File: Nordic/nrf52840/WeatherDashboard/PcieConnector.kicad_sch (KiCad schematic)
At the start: 2 parts

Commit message: pcie connector
Add connectins to the pcie connector
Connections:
- net EPD_SCK: now reaches J4.14
- net EPD_DIN: now reaches J4.18
- net ~{EPD_CS}: now reaches J4.20
- net EPD_DC: now reaches J4.22
- net EPD_BUSY: now reaches J4.24
- net SDA: now reaches J4.25
- net ~{EPD_RST}: now reaches J4.26
- net SCL: now reaches J4.27
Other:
- moved on the sheet: R8
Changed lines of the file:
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@@
+	(wire
+		(pts
+			(xy 152.4 88.9) (xy 144.78 88.9)
+		)
+		(stroke
+			(width 0)
+			(type default)
+		)
+	)
 	(wire
 		(pts
@@
 	(wire
 		(pts
+			(xy 152.4 78.74) (xy 144.78 78.74)
+		)
+		(stroke
+			(width 0)
+			(type default)
+		)
+	)
+	(wire
+		(pts
+			(xy 152.4 86.36) (xy 144.78 86.36)
+		)
+		(stroke
+			(width 0)
+			(type default)
+		)
+	)
+	(wire
+		(pts
 			(xy 144.78 121.92) (xy 152.4 121.92)
 		)
@@
 	(wire
 		(pts
+			(xy 152.4 93.98) (xy 144.78 93.98)
+		)
+		(stroke
+			(width 0)
+			(type default)
+		)
+	)
+	(wire
+		(pts
+			(xy 128.27 93.98) (xy 134.62 93.98)
+		)
+		(stroke
+			(width 0)
+			(type default)
+		)
+	)
+	(wire
+		(pts
 			(xy 144.78 63.5) (xy 144.78 66.04)
 		)
@@
 	(wire
 		(pts
+			(xy 128.27 96.52) (xy 134.62 96.52)
+		)
+		(stroke
+			(width 0)
+			(type default)
+		)
+	)
+	(wire
+		(pts
 			(xy 144.78 116.84) (xy 144.78 119.38)
 		)
@@
 	(wire
 		(pts
-			(xy 162.56 73.66) (xy 162.56 72.39)
+			(xy 170.18 73.66) (xy 170.18 72.39)
 		)
 		(stroke
@@
 	(wire
 		(pts
-			(xy 144.78 81.28) (xy 162.56 81.28)
+			(xy 144.78 81.28) (xy 170.18 81.28)
 		)
 		(stroke
@@
 	(wire
 		(pts
+			(xy 152.4 83.82) (xy 144.78 83.82)
+		)
+		(stroke
+			(width 0)
+			(type default)
+		)
+	)
+	(wire
+		(pts
+			(xy 144.78 91.44) (xy 152.4 91.44)
+		)
+		(stroke
+			(width 0)
+			(type default)
+		)
+	)
+	(wire
+		(pts
 			(xy 144.78 124.46) (xy 144.78 127)
 		)
@@
 	(wire
 		(pts
-			(xy 162.56 72.39) (xy 166.37 72.39)
+			(xy 170.18 72.39) (xy 166.37 72.39)
 		)
 		(stroke
@@
 		)
 	)
+	(hierarchical_label "~{EPD_CS}"
+		(shape input)
+		(at 152.4 86.36 0)
+		(effects
+			(font
+				(size 1.27 1.27)
+			)
+			(justify left)
+		)
+	)
+	(hierarchical_label "EPD_DC"
+		(shape input)
+		(at 152.4 88.9 0)
+		(effects
+			(font
+				(size 1.27 1.27)
+			)
+			(justify left)
+		)
+	)
 	(hierarchical_label "GND"
 		(shape input)
 		(at 153.67 63.5 0)
+		(effects
+			(font
+				(size 1.27 1.27)
+			)
+			(justify left)
+		)
+	)
+	(hierarchical_label "SDA"
+		(shape input)
+		(at 128.27 93.98 180)
+		(effects
+			(font
+				(size 1.27 1.27)
+			)
+			(justify right)
+		)
+	)
+	(hierarchical_label "EPD_BUSY"
+		(shape input)
+		(at 152.4 91.44 0)
+		(effects
+			(font
+				(size 1.27 1.27)
+			)
+			(justify left)
+		)
+	)
+	(hierarchical_label "EPD_SCK"
+		(shape input)
+		(at 152.4 78.74 0)
+		(effects
+			(font
+				(size 1.27 1.27)
+			)
+			(justify left)
+		)
+	)
+	(hierarchical_label "SCL"
+		(shape input)
+		(at 128.27 96.52 180)
+		(effects
+			(font
+				(size 1.27 1.27)
+			)
+			(justify right)
+		)
+	)
+	(hierarchical_label "EPD_DIN"
+		(shape input)
+		(at 152.4 83.82 0)
+		(effects
+			(font
+				(size 1.27 1.27)
+			)
+			(justify left)
+		)
+	)
+	(hierarchical_label "~{EPD_RST}"
+		(shape input)
+		(at 152.4 93.98 0)
 		(effects
 			(font
@@
 	(symbol
 		(lib_id "Device:R_US")
-		(at 162.56 77.47 0)
+		(at 170.18 77.47 0)
 		(unit 1)
 		(exclude_from_sim no)
@@
 		(fields_autoplaced yes)
 		(property "Reference" "R8"
-			(at 165.1 76.1999 0)
+			(at 172.72 76.1999 0)
 			(effects
 				(font
@@
 		)
 		(property "Value" "10K"
-			(at 165.1 78.7399 0)
+			(at 172.72 78.7399 0)
 			(effects
 				(font
@@
 		)
 		(property "Footprint" "Resistor_SMD:R_0402_1005Metric_Pad0.72x0.64mm_HandSolder"
-			(at 163.576 77.724 90)
+			(at 171.196 77.724 90)
 			(effects
 				(font
@@
 		)
 		(property "Datasheet" "~"
-			(at 162.56 77.47 0)
+			(at 170.18 77.47 0)
 			(effects
 				(font
@@
 		)
 		(property "Description" "Resistor, US symbol"
-			(at 162.56 77.47 0)
+			(at 170.18 77.47 0)
 			(effects
 				(font

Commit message: Layout
layout update
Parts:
- added C14: C, Capacitor_SMD:C_0805_2012Metric_Pad1.18x1.45mm_HandSolder, symbol Device:C
- added J5: Conn_01x03_Pin, Connector_PinSocket_2.54mm:PinSocket_1x03_P2.54mm_Vertical, symbol Connector:Conn_01x03_Pin
- added S1: 436331045822, User_Footprint:4363X10458XX, symbol _Misc_Symbols:436331045822
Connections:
- net GND: now also C14.2, J5.3 (Pin_3), S1.4
- net at J4.16, R8.2: now also C14.1, S1.3
- net at J4.5: now also J5.1 (Pin_1)
- net at J4.7: now also J5.2 (Pin_2)
- no-connect marks 0 -> 29

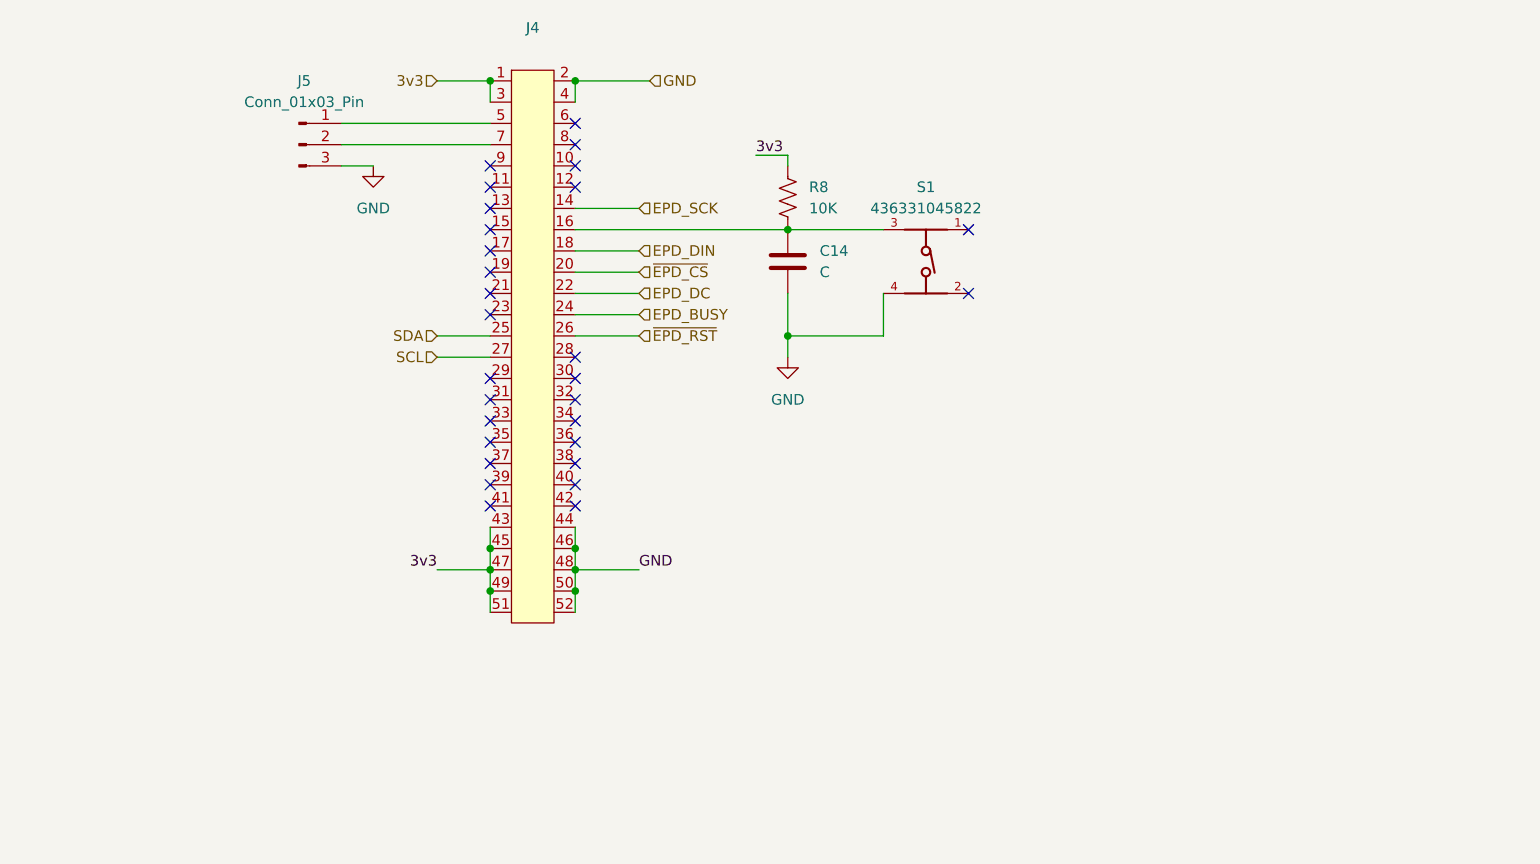
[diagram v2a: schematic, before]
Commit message: layout
Start weather station layout
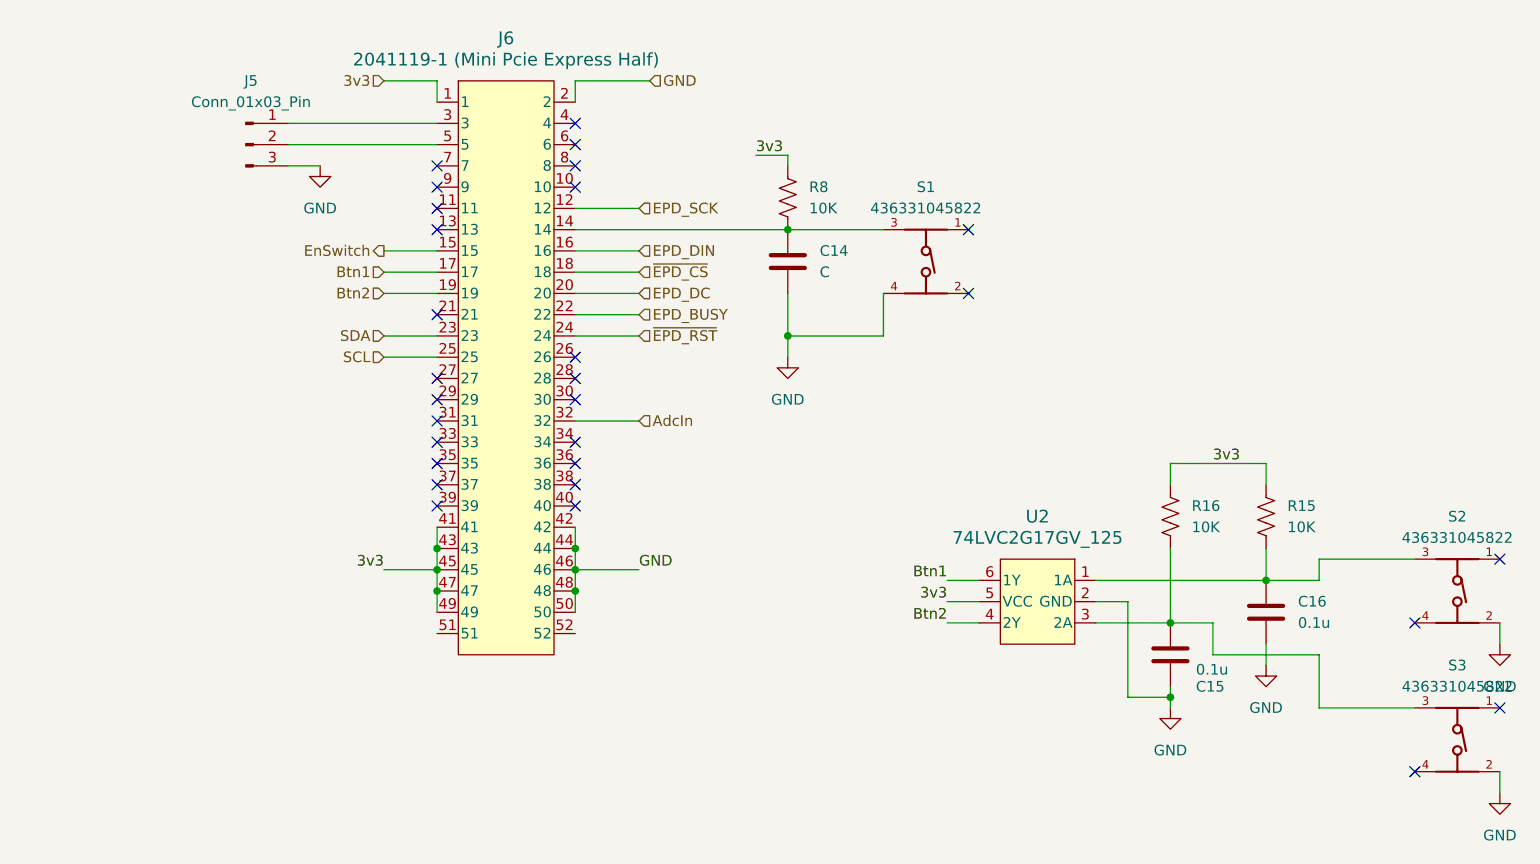
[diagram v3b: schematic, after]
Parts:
- removed J4: ~, User_Footprint:Mini PCI express Half, symbol Cards:Mini_PCIexpress_Half
- added C15, C16: 0.1u, Capacitor_SMD:C_0402_1005Metric_Pad0.74x0.62mm_HandSolder, symbol Device:C
- added J6: 2041119-1 (Mini Pcie Express Half), User_Footprint:CONN_2041119-1_TEC, symbol _Connectors:2041119-1
- added R15, R16: 10K, Resistor_SMD:R_0402_1005Metric_Pad0.72x0.64mm_HandSolder, symbol Device:R_US
- added S2, S3: 436331045822, User_Footprint:4363X10458XX, symbol _Misc_Symbols:436331045822
- added U2: 74LVC2G17GV_125, User_Footprint:SC-74_TSOP6_NEX, symbol _Misc_Symbols:74LVC2G17GV_125
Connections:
- net 3v3: now also J6.1, J6.41, J6.43, J6.45, J6.47, J6.49, R15.1, R16.1, U2.5 (VCC)
- net EPD_BUSY: now also J6.22
- net EPD_DC: now also J6.20
- net EPD_DIN: now also J6.16
- net EPD_SCK: now also J6.12
- net GND: now also C15.2, C16.2, J6.2, J6.42, J6.44, J6.46, J6.48, J6.50, S2.2, S3.2, U2.2 (GND)
- net SCL: now also J6.25
- net SDA: now also J6.23
- net ~{EPD_CS}: now also J6.18
- net ~{EPD_RST}: now also J6.24
- net at J5.1 (Pin_1): now also J6.3
- net at J5.2 (Pin_2): now also J6.5
- net at C14.1, R8.2, S1.3: now also J6.14
- new net: C16.1, R15.2, S2.3, U2.1 (1A)
- new net: C15.1, R16.2, S3.3, U2.3 (2A)
- new net AdcIn: J6.32
- new net Btn1: J6.17, U2.6 (1Y)
- new net Btn2: J6.19, U2.4 (2Y)
- new net EnSwitch: J6.15
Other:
- moved on the sheet: J5

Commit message: layout
update layout for the pcie connector
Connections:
- net EPD_BUSY: now also J6.7; no longer J6.22
- net EPD_DC: now also J6.11; no longer J6.20
- net ~{EPD_CS}: now also J6.13; no longer J6.18
- net ~{EPD_RST}: now also J6.9; no longer J6.24
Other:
- moved on the sheet: J5
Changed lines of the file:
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@@
-	)
-	(no_connect
-		(at 128.27 78.74)
 	)
 	(no_connect
@@
 	)
 	(no_connect
-		(at 128.27 73.66)
+		(at 144.78 91.44)
 	)
 	(no_connect
@@
 	)
 	(no_connect
-		(at 128.27 76.2)
+		(at 144.78 86.36)
 	)
 	(no_connect
@@
 	)
 	(no_connect
-		(at 128.27 81.28)
+		(at 144.78 88.9)
 	)
 	(no_connect
@@
 	)
 	(no_connect
+		(at 144.78 93.98)
+	)
+	(no_connect
 		(at 144.78 111.76)
 	)
@@
 	(wire
 		(pts
-			(xy 152.4 88.9) (xy 144.78 88.9)
-		)
-		(stroke
-			(width 0)
-			(type default)
-		)
-	)
-	(wire
-		(pts
 			(xy 121.92 63.5) (xy 128.27 63.5)
 		)
@@
 	(wire
 		(pts
+			(xy 121.92 78.74) (xy 128.27 78.74)
+		)
+		(stroke
+			(width 0)
+			(type default)
+		)
+	)
+	(wire
+		(pts
 			(xy 227.33 109.22) (xy 227.33 111.76)
 		)
@@
 	(wire
 		(pts
-			(xy 152.4 86.36) (xy 144.78 86.36)
-		)
-		(stroke
-			(width 0)
-			(type default)
-		)
-	)
-	(wire
-		(pts
 			(xy 144.78 121.92) (xy 152.4 121.92)
 		)
@@
 	(wire
 		(pts
-			(xy 152.4 93.98) (xy 144.78 93.98)
-		)
-		(stroke
-			(width 0)
-			(type default)
-		)
-	)
-	(wire
-		(pts
 			(xy 128.27 119.38) (xy 128.27 121.92)
 		)
@@
 	(wire
 		(pts
+			(xy 121.92 81.28) (xy 128.27 81.28)
+		)
+		(stroke
+			(width 0)
+			(type default)
+		)
+	)
+	(wire
+		(pts
 			(xy 207.01 125.73) (xy 210.82 125.73)
 		)
@@
 	(wire
 		(pts
+			(xy 121.92 76.2) (xy 128.27 76.2)
+		)
+		(stroke
+			(width 0)
+			(type default)
+		)
+	)
+	(wire
+		(pts
 			(xy 144.78 63.5) (xy 153.67 63.5)
 		)
@@
 	(wire
 		(pts
-			(xy 110.49 68.58) (xy 128.27 68.58)
+			(xy 91.44 68.58) (xy 128.27 68.58)
 		)
 		(stroke
@@
 	(wire
 		(pts
+			(xy 121.92 73.66) (xy 128.27 73.66)
+		)
+		(stroke
+			(width 0)
+			(type default)
+		)
+	)
+	(wire
+		(pts
 			(xy 215.9 111.76) (xy 215.9 109.22)
 		)
@@
 	(wire
 		(pts
-			(xy 110.49 73.66) (xy 114.3 73.66)
-		)
-		(stroke
-			(width 0)
-			(type default)
-		)
-	)
-	(wire
-		(pts
-			(xy 110.49 71.12) (xy 128.27 71.12)
+			(xy 91.44 73.66) (xy 95.25 73.66)
+		)
+		(stroke
+			(width 0)
+			(type default)
+		)
+	)
+	(wire
+		(pts
+			(xy 91.44 71.12) (xy 128.27 71.12)
 		)
 		(stroke
@@
 		(pts
 			(xy 215.9 109.22) (xy 227.33 109.22)
-		)
-		(stroke
-			(width 0)
-			(type default)
-		)
-	)
-	(wire
-		(pts
-			(xy 144.78 91.44) (xy 152.4 91.44)
 		)
 		(stroke
@@
 	(hierarchical_label "~{EPD_CS}"
 		(shape input)
-		(at 152.4 86.36 0)
+		(at 121.92 81.28 180)
+		(effects
+			(font
+				(size 1.27 1.27)
+			)
+			(justify right)
+		)
+	)
+	(hierarchical_label "EPD_DC"
+		(shape input)
+		(at 121.92 78.74 180)
+		(effects
+			(font
+				(size 1.27 1.27)
+			)
+			(justify right)
+		)
+	)
+	(hierarchical_label "Btn1"
+		(shape input)
+		(at 121.92 86.36 180)
+		(effects
+			(font
+				(size 1.27 1.27)
+			)
+			(justify right)
+		)
+	)
+	(hierarchical_label "GND"
+		(shape input)
+		(at 153.67 63.5 0)
 		(effects
 			(font
@@
 		)
 	)
-	(hierarchical_label "EPD_DC"
-		(shape input)
-		(at 152.4 88.9 0)
+	(hierarchical_label "SDA"
+		(shape input)
+		(at 121.92 93.98 180)
+		(effects
+			(font
+				(size 1.27 1.27)
+			)
+			(justify right)
+		)
+	)
+	(hierarchical_label "Btn2"
+		(shape input)
+		(at 121.92 88.9 180)
+		(effects
+			(font
+				(size 1.27 1.27)
+			)
+			(justify right)
+		)
+	)
+	(hierarchical_label "EPD_BUSY"
+		(shape input)
+		(at 121.92 73.66 180)
+		(effects
+			(font
+				(size 1.27 1.27)
+			)
+			(justify right)
+		)
+	)
+	(hierarchical_label "EPD_SCK"
+		(shape input)
+		(at 152.4 78.74 0)
 		(effects
 			(font
@@
 		)
 	)
-	(hierarchical_label "Btn1"
-		(shape input)
-		(at 121.92 86.36 180)
+	(hierarchical_label "SCL"
+		(shape input)
+		(at 121.92 96.52 180)
 		(effects
 			(font
@@
 		)
 	)
-	(hierarchical_label "GND"
-		(shape input)
-		(at 153.67 63.5 0)
+	(hierarchical_label "EPD_DIN"
+		(shape input)
+		(at 152.4 83.82 0)
 		(effects
 			(font
@@
 		)
 	)
-	(hierarchical_label "SDA"
-		(shape input)
-		(at 121.92 93.98 180)
+	(hierarchical_label "~{EPD_RST}"
+		(shape input)
+		(at 121.92 76.2 180)
 		(effects
 			(font
@@
 			)
 			(justify right)
-		)
-	)
-	(hierarchical_label "Btn2"
-		(shape input)
-		(at 121.92 88.9 180)
-		(effects
-			(font
-				(size 1.27 1.27)
-			)
-			(justify right)
-		)
-	)
-	(hierarchical_label "EPD_BUSY"
-		(shape input)
-		(at 152.4 91.44 0)
-		(effects
-			(font
-				(size 1.27 1.27)
-			)
-			(justify left)
-		)
-	)
-	(hierarchical_label "EPD_SCK"
-		(shape input)
-		(at 152.4 78.74 0)
-		(effects
-			(font
-				(size 1.27 1.27)
-			)
-			(justify left)
-		)
-	)
-	(hierarchical_label "SCL"
-		(shape input)
-		(at 121.92 96.52 180)
-		(effects
-			(font
-				(size 1.27 1.27)
-			)
-			(justify right)
-		)
-	)
-	(hierarchical_label "EPD_DIN"
-		(shape input)
-		(at 152.4 83.82 0)
-		(effects
-			(font
-				(size 1.27 1.27)
-			)
-			(justify left)
-		)
-	)
-	(hierarchical_label "~{EPD_RST}"
-		(shape input)
-		(at 152.4 93.98 0)
-		(effects
-			(font
-				(size 1.27 1.27)
-			)
-			(justify left)
 		)
 	)
@@
 	(symbol
 		(lib_id "power:GND")
-		(at 114.3 73.66 0)
+		(at 95.25 73.66 0)
 		(unit 1)
 		(exclude_from_sim no)
@@
 		(fields_autoplaced yes)
 		(property "Reference" "#PWR016"
-			(at 114.3 80.01 0)
+			(at 95.25 80.01 0)
 			(effects
 				(font
@@
 		)
 		(property "Value" "GND"
-			(at 114.3 78.74 0)
+			(at 95.25 78.74 0)
 			(effects
 				(font
@@
 		)
 		(property "Footprint" ""
-			(at 114.3 73.66 0)
+			(at 95.25 73.66 0)
 			(effects
 				(font
@@
 		)
 		(property "Datasheet" ""
-			(at 114.3 73.66 0)
+			(at 95.25 73.66 0)
 			(effects
 				(font
@@
 		)
 		(property "Description" "Power symbol creates a global label with name \"GND\" , ground"
-			(at 114.3 73.66 0)
+			(at 95.25 73.66 0)
 			(effects
 				(font
@@
 	(symbol
 		(lib_id "Connector:Conn_01x03_Pin")
-		(at 105.41 71.12 0)
+		(at 86.36 71.12 0)
 		(unit 1)
 		(exclude_from_sim no)
@@
 		(fields_autoplaced yes)
 		(property "Reference" "J5"
-			(at 106.045 63.5 0)
+			(at 86.995 63.5 0)
 			(effects
 				(font
@@
 		)
 		(property "Value" "Conn_01x03_Pin"
-			(at 106.045 66.04 0)
+			(at 86.995 66.04 0)
 			(effects
 				(font
@@
 		)
 		(property "Footprint" "Connector_PinSocket_2.54mm:PinSocket_1x03_P2.54mm_Vertical"
-			(at 105.41 71.12 0)
+			(at 86.36 71.12 0)
 			(effects
 				(font
@@
 		)
 		(property "Datasheet" "~"
-			(at 105.41 71.12 0)
+			(at 86.36 71.12 0)
 			(effects
 				(font
@@
 		)
 		(property "Description" "Generic connector, single row, 01x03, script generated"
-			(at 105.41 71.12 0)
-			(effects
-				(font
+			(at 86.36 71.12 0)
+			(effects
+				(font
